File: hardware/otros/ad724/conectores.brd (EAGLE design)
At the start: 24.1 x 39 mm, 5 parts, among them U1 MINI-DIN6PTH

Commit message: planos de masa
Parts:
- moved JP1 31.9 mm to (33.0, 3.81), turned to 90 degrees
- moved U1 18.5 mm to (6.99, 0.00), turned to 180 degrees
- moved JP3 15.3 mm to (20.3, 5.08), turned to 90 degrees
- moved X1 15.3 mm to (19.1, 20.3), turned to 0 degrees
- moved JP2 11.1 mm to (19.1, 14.6), turned to 0 degrees
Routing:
- net N$11: track 23.4 -> 22.6 mm
- net N$3: track 6.78 -> 7.42 mm
- net N$2: track 11.4 -> 12.0 mm
- net N$4: track 4.81 -> 5.44 mm
- net N$10: track 15.0 -> 14.3 mm
- net N$1: track 4.52 -> 5.16 mm
- net N$9: track 22.1 -> 21.4 mm
- added copper zone on layer 16, net GND
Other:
- board size 24.1 x 39 mm -> 39 x 24.1 mm

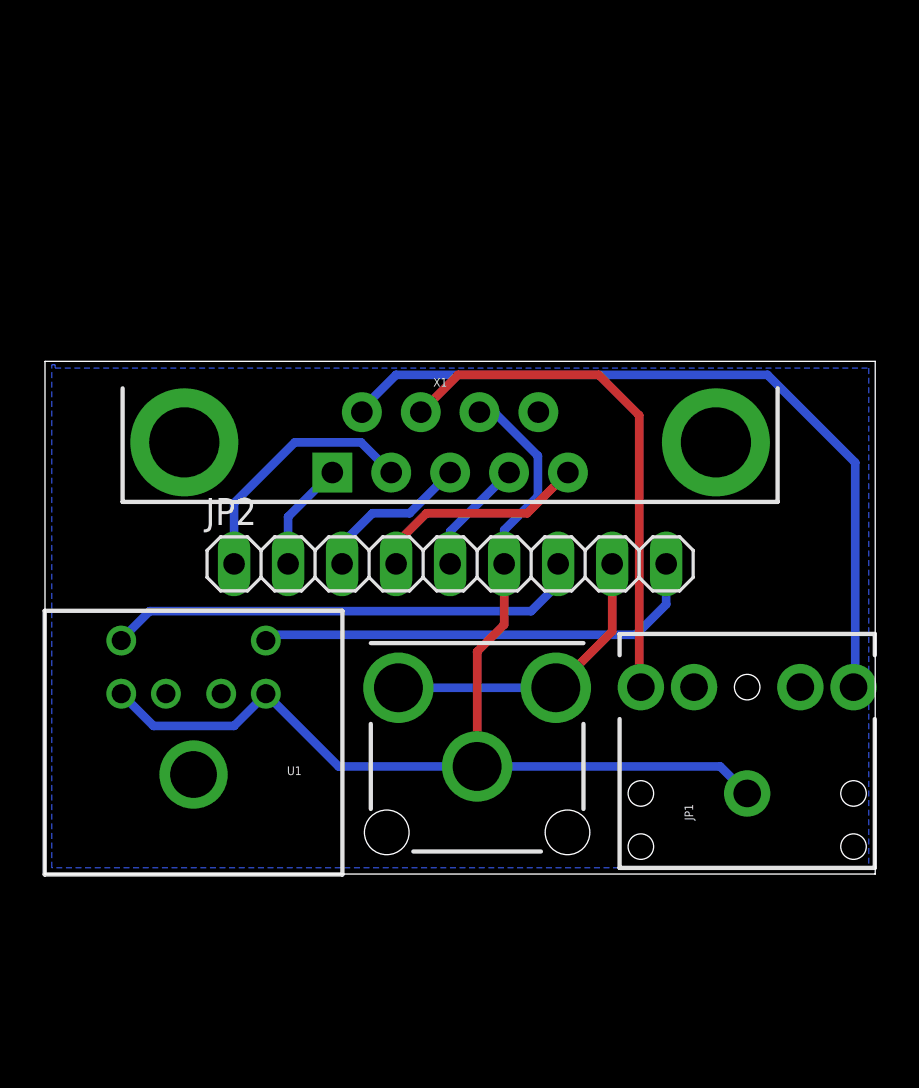
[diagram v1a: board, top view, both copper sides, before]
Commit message: 
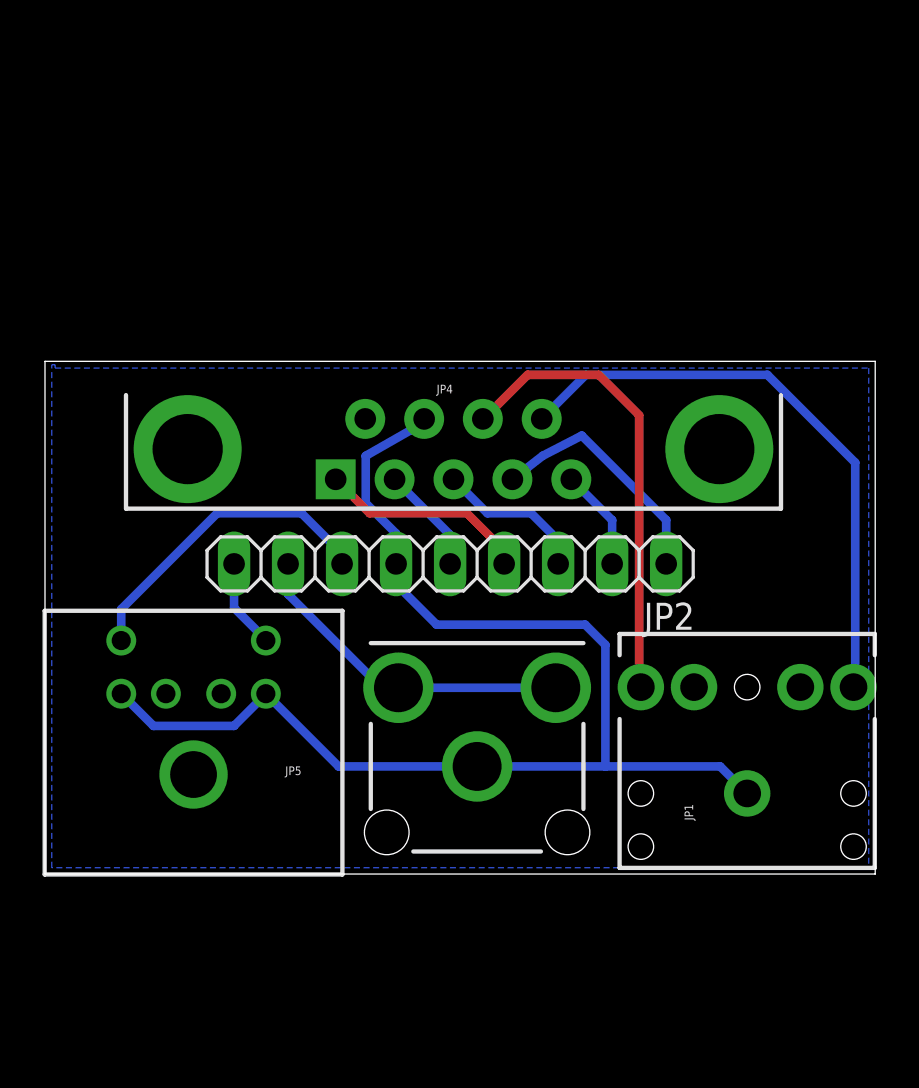
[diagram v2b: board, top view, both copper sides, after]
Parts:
- removed X1: (no value), SparkFun-Connectors:DB9
- added JP4: (no value), SparkFun-Connectors:DB9_MALE
- turned JP2 to 180 degrees
- renumbered U1 to JP5
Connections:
- removed net N$8: JP1.SLEEVE, JP2.6, JP3.SHELL, JP5.3, JP5.4, X1.8
- new net GND: JP1.SLEEVE, JP2.6, JP3.SHELL, JP4.8, JP5.3, JP5.4
- net N$1: now also JP4.1; no longer X1.1
- net N$2: now also JP4.2; no longer X1.2
- net N$3: now also JP4.3; no longer X1.3
- net N$4: now also JP4.4; no longer X1.4
- net N$5: now also JP4.5; no longer X1.5
- net N$6: now also JP4.6; no longer X1.6
- net N$7: now also JP4.7; no longer X1.7
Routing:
- net GND: track 0.00 -> 59.3 mm
- net N$8: track 52.0 -> 0.00 mm
- net N$9: track 21.4 -> 4.22 mm
- net N$6: track 36.3 -> 27.9 mm
- net N$11: track 22.6 -> 15.0 mm
- net N$7: track 24.6 -> 21.8 mm
- net N$10: track 14.3 -> 15.8 mm

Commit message: 
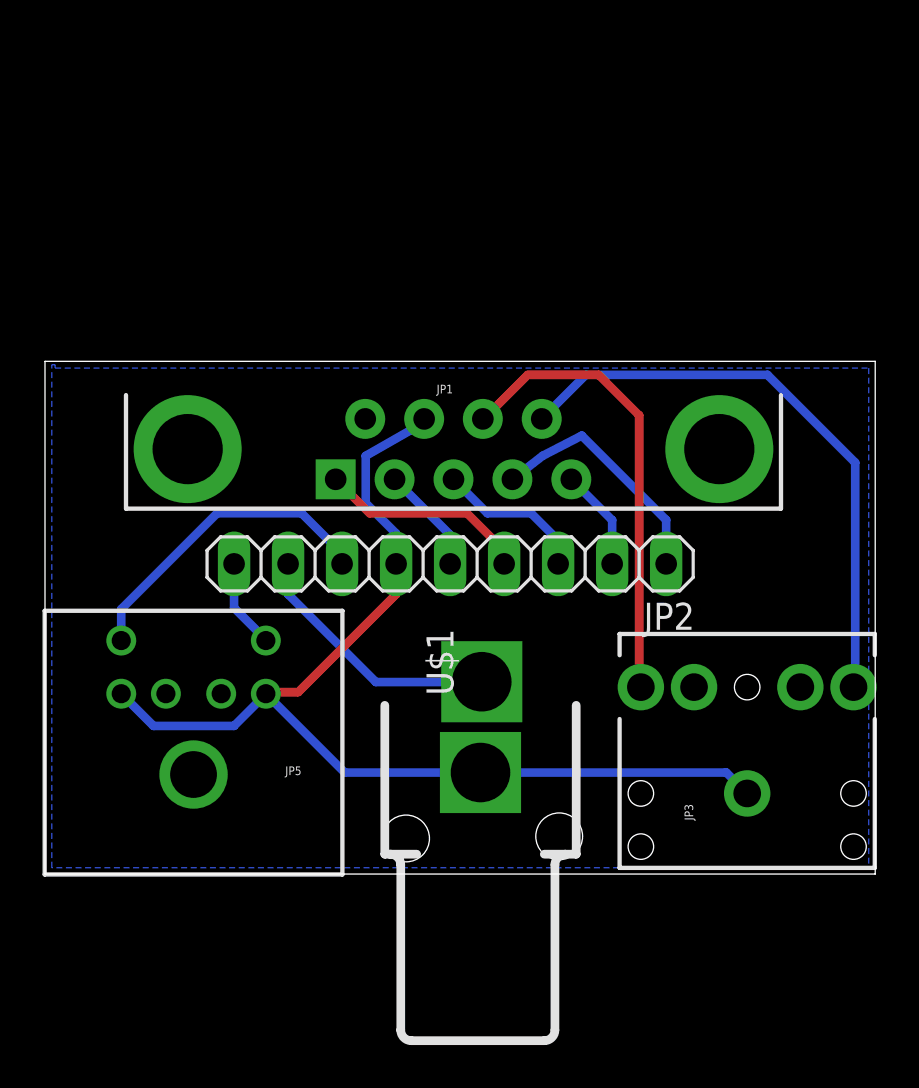
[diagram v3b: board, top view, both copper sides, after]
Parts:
- removed JP4: (no value), SparkFun-Connectors:DB9_MALE
- added U$1: RCA_FEMALE, Mio:RCA_EBAY
- JP1: device SparkFun-Connectors:AUDIO-JACK -> SparkFun-Connectors:DB9_MALE
- JP3: value RCA -> (none); device SparkFun-Connectors:RCA -> SparkFun-Connectors:AUDIO-JACK
- moved JP1 21.3 mm to (19.2, 20.0), turned to 0 degrees
- moved JP3 12.8 mm to (33.0, 3.81)
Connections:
- net GND: now also JP1.8, JP3.SLEEVE, U$1.1; no longer JP1.SLEEVE, JP3.SHELL, JP4.8
- net N$1: now also JP1.1; no longer JP4.1
- net N$10: now also U$1.2; no longer JP3.PIN, JP3.SWITCH
- net N$2: now also JP1.2; no longer JP4.2
- net N$3: now also JP1.3; no longer JP4.3
- net N$4: now also JP1.4; no longer JP4.4
- net N$5: now also JP1.5; no longer JP4.5
- net N$6: now also JP1.6, JP3.TIP; no longer JP1.TIP, JP4.6
- net N$7: now also JP1.7, JP3.RING; no longer JP1.RING, JP4.7
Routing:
- net GND: track 59.3 -> 51.1 mm
- net N$10: track 15.8 -> 12.3 mm
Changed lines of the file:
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@@
 <layer number="113" name="IDFDebug" color="4" fill="1" visible="yes" active="yes"/>
 <layer number="116" name="Patch_BOT" color="9" fill="4" visible="yes" active="yes"/>
+<layer number="118" name="Rect_Pads" color="7" fill="1" visible="yes" active="yes"/>
 <layer number="121" name="_tsilk" color="7" fill="1" visible="yes" active="yes"/>
 <layer number="122" name="_bsilk" color="7" fill="1" visible="yes" active="yes"/>
@@
 </autorouter>
 <elements>
-<element name="JP1" library="SparkFun-Connectors" package="AUDIO-JACK" value="" x="33.02" y="3.81" rot="R90"/>
+<element name="JP3" library="SparkFun-Connectors" package="AUDIO-JACK" value="" x="33.02" y="3.81" rot="R90"/>
 <element name="JP5" library="SparkFun-Connectors" package="MINI-DIN6" value="MINI-DIN6PTH" x="6.985" y="0" rot="R180"/>
 <element name="JP2" library="pinhead" package="1X09" value="" x="19.05" y="14.605" rot="R180"/>
-<element name="JP3" library="SparkFun-Connectors" package="RCA" value="RCA" x="20.32" y="5.08" rot="R90"/>
-<element name="JP4" library="SparkFun-Connectors" package="DB9_MALE" value="" x="19.20875" y="20.0025"/>
+<element name="JP1" library="SparkFun-Connectors" package="DB9_MALE" value="" x="19.20875" y="20.0025"/>
+<element name="U$1" library="Mio" package="RCA_EBAY" value="RCA_FEMALE" x="20.47875" y="0.79375" rot="R90"/>
 </elements>
 <signals>
 <signal name="N$1">
 <contactref element="JP2" pad="2"/>
-<contactref element="JP4" pad="1"/>
+<contactref element="JP1" pad="1"/>
 <wire x1="26.67" y1="14.605" x2="26.67" y2="16.66125" width="0.4064" layer="16"/>
 <wire x1="26.67" y1="16.66125" x2="24.74875" y2="18.5825" width="0.4064" layer="16"/>
@@
 <signal name="N$2">
 <contactref element="JP2" pad="1"/>
-<contactref element="JP4" pad="2"/>
+<contactref element="JP1" pad="2"/>
 <wire x1="29.21" y1="14.605" x2="29.21" y2="16.66875" width="0.4064" layer="16"/>
 <wire x1="29.21" y1="16.66875" x2="25.24125" y2="20.6375" width="0.4064" layer="16"/>
@@
 <signal name="N$3">
 <contactref element="JP2" pad="3"/>
-<contactref element="JP4" pad="3"/>
+<contactref element="JP1" pad="3"/>
 <wire x1="24.13" y1="14.605" x2="24.13" y2="15.71625" width="0.4064" layer="16"/>
 <wire x1="24.13" y1="15.71625" x2="22.86" y2="16.98625" width="0.4064" layer="16"/>
@@
 <signal name="N$4">
 <contactref element="JP2" pad="5"/>
-<contactref element="JP4" pad="4"/>
+<contactref element="JP1" pad="4"/>
 <wire x1="19.05" y1="14.605" x2="19.05" y2="15.97125" width="0.4064" layer="16"/>
 <wire x1="19.05" y1="15.97125" x2="16.43875" y2="18.5825" width="0.4064" layer="16"/>
@@
 <signal name="N$5">
 <contactref element="JP2" pad="4"/>
-<contactref element="JP4" pad="5"/>
+<contactref element="JP1" pad="5"/>
 <wire x1="21.59" y1="14.605" x2="21.59" y2="15.24" width="0.4064" layer="1"/>
 <wire x1="21.59" y1="15.24" x2="19.84375" y2="16.98625" width="0.4064" layer="1"/>
@@
 </signal>
 <signal name="N$6">
-<contactref element="JP1" pad="TIP"/>
+<contactref element="JP3" pad="TIP"/>
 <wire x1="33.9725" y1="23.495" x2="38.1" y2="19.3675" width="0.4064" layer="16"/>
 <wire x1="38.1" y1="19.3675" x2="38.1" y2="8.89" width="0.4064" layer="16"/>
 <wire x1="38.1" y1="8.89" x2="38.02" y2="8.81" width="0.4064" layer="16"/>
-<contactref element="JP4" pad="6"/>
+<contactref element="JP1" pad="6"/>
 <wire x1="33.9725" y1="23.495" x2="25.43125" y2="23.495" width="0.4064" layer="16"/>
 <wire x1="25.43125" y1="23.495" x2="23.35875" y2="21.4225" width="0.4064" layer="16"/>
 </signal>
 <signal name="N$7">
-<contactref element="JP1" pad="RING"/>
+<contactref element="JP3" pad="RING"/>
 <wire x1="28.02" y1="8.81" x2="27.94" y2="8.89" width="0.4064" layer="1"/>
 <wire x1="27.94" y1="8.89" x2="27.94" y2="21.59" width="0.4064" layer="1"/>
 <wire x1="27.94" y1="21.59" x2="26.035" y2="23.495" width="0.4064" layer="1"/>
-<contactref element="JP4" pad="7"/>
+<contactref element="JP1" pad="7"/>
 <wire x1="20.58875" y1="21.4225" x2="20.62875" y2="21.4225" width="0.4064" layer="1"/>
 <wire x1="20.62875" y1="21.4225" x2="22.70125" y2="23.495" width="0.4064" layer="1"/>
@@
 <signal name="N$10">
 <contactref element="JP2" pad="8"/>
-<contactref element="JP3" pad="PIN"/>
-<contactref element="JP3" pad="SWITCH"/>
-<wire x1="24.02" y1="8.78" x2="16.62" y2="8.78" width="0.4064" layer="16"/>
-<wire x1="16.62" y1="8.78" x2="15.82625" y2="8.78" width="0.4064" layer="16"/>
-<wire x1="15.82625" y1="8.78" x2="11.43" y2="13.17625" width="0.4064" layer="16"/>
 <wire x1="11.43" y1="13.17625" x2="11.43" y2="14.605" width="0.4064" layer="16"/>
+<contactref element="U$1" pad="2"/>
+<wire x1="11.43" y1="13.17625" x2="15.5575" y2="9.04875" width="0.4064" layer="16"/>
+<wire x1="15.5575" y1="9.04875" x2="20.52375" y2="9.04875" width="0.4064" layer="16"/>
+<wire x1="20.52375" y1="9.04875" x2="20.53875" y2="9.06375" width="0.4064" layer="16"/>
 </signal>
 <signal name="N$9">
@@
 <vertex x="0.47625" y="23.97125"/>
 </polygon>
-<contactref element="JP1" pad="SLEEVE"/>
+<contactref element="JP3" pad="SLEEVE"/>
 <contactref element="JP2" pad="6"/>
 <contactref element="JP5" pad="3"/>
 <contactref element="JP5" pad="4"/>
-<contactref element="JP3" pad="SHELL"/>
-<wire x1="33.02" y1="3.81" x2="31.75" y2="5.08" width="0.4064" layer="16"/>
-<wire x1="31.75" y1="5.08" x2="26.3525" y2="5.08" width="0.4064" layer="16"/>
-<wire x1="26.3525" y1="5.08" x2="20.32" y2="5.08" width="0.4064" layer="16"/>
-<wire x1="13.805" y1="5.08" x2="10.385" y2="8.5" width="0.4064" layer="16"/>
+<wire x1="14.09125" y1="4.79375" x2="10.385" y2="8.5" width="0.4064" layer="16"/>
 <wire x1="10.385" y1="8.5" x2="10.385" y2="8.48" width="0.4064" layer="16"/>
 <wire x1="10.385" y1="8.48" x2="8.89" y2="6.985" width="0.4064" layer="16"/>
 <wire x1="8.89" y1="6.985" x2="5.1" y2="6.985" width="0.4064" layer="16"/>
 <wire x1="5.1" y1="6.985" x2="3.585" y2="8.5" width="0.4064" layer="16"/>
-<wire x1="20.32" y1="5.08" x2="13.805" y2="5.08" width="0.4064" layer="16"/>
-<contactref element="JP4" pad="8"/>
+<contactref element="JP1" pad="8"/>
 <wire x1="16.51" y1="14.605" x2="16.51" y2="16.03375" width="0.4064" layer="16"/>
 <wire x1="16.51" y1="16.03375" x2="15.08125" y2="17.4625" width="0.4064" layer="16"/>
@@
 <wire x1="17.30375" y1="20.955" x2="17.82" y2="21.43125" width="0.4064" layer="16"/>
 <wire x1="17.82" y1="21.43125" x2="17.82875" y2="21.4225" width="0.4064" layer="16"/>
-<wire x1="16.51" y1="14.605" x2="16.51" y2="13.6525" width="0.4064" layer="16"/>
-<wire x1="16.51" y1="13.6525" x2="18.415" y2="11.7475" width="0.4064" layer="16"/>
-<wire x1="18.415" y1="11.7475" x2="25.4" y2="11.7475" width="0.4064" layer="16"/>
-<wire x1="25.4" y1="11.7475" x2="26.3525" y2="10.795" width="0.4064" layer="16"/>
-<wire x1="26.3525" y1="10.795" x2="26.3525" y2="5.08" width="0.4064" layer="16"/>
+<contactref element="U$1" pad="1"/>
+<wire x1="20.47875" y1="4.79375" x2="14.09125" y2="4.79375" width="0.4064" layer="16"/>
+<wire x1="16.51" y1="14.605" x2="16.51" y2="13.17625" width="0.4064" layer="1"/>
+<wire x1="16.51" y1="13.17625" x2="11.90625" y2="8.5725" width="0.4064" layer="1"/>
+<wire x1="11.90625" y1="8.5725" x2="10.4575" y2="8.5725" width="0.4064" layer="1"/>
+<wire x1="10.4575" y1="8.5725" x2="10.385" y2="8.5" width="0.4064" layer="1"/>
+<wire x1="20.47875" y1="4.79375" x2="32.03625" y2="4.79375" width="0.4064" layer="16"/>
+<wire x1="32.03625" y1="4.79375" x2="33.02" y2="3.81" width="0.4064" layer="16"/>
 </signal>
 </signals>
